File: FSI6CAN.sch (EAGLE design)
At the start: 39 parts, among them IC2 TCAN332DR, IC3 ATMEGA328P, IC4 MCP2515

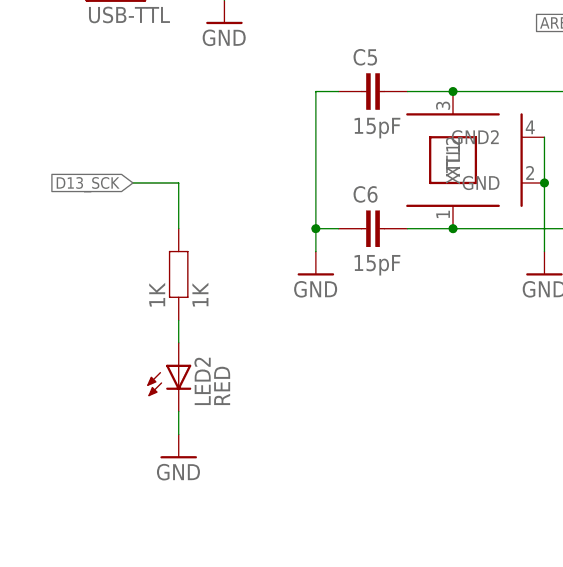
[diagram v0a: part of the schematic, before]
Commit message: Fixed value of R10
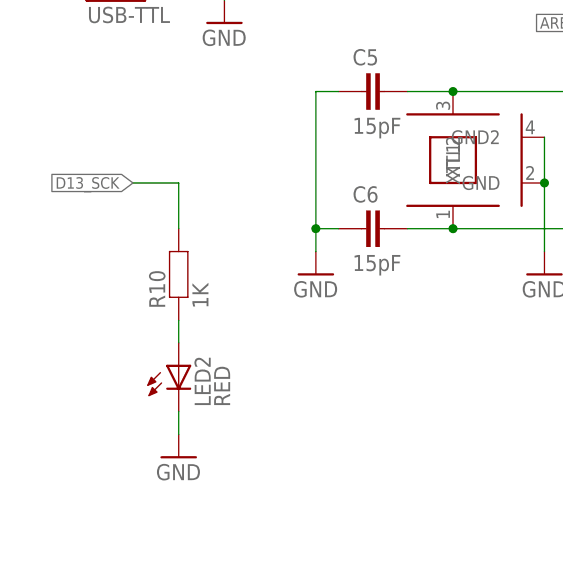
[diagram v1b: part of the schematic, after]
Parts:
- renumbered 1K to R10
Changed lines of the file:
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@@
 <?xml version="1.0" encoding="utf-8"?>
 <!DOCTYPE eagle SYSTEM "eagle.dtd">
-<eagle version="9.5.0">
+<eagle version="9.5.2">
 <drawing>
 <settings>
@@
 <part name="LED2" library="SuperHouse-LEDs" library_urn="urn:adsk.eagle:library:11790571" deviceset="LED" device="0603" package3d_urn="urn:adsk.eagle:package:7066240/3" value="RED"/>
 <part name="GND12" library="SuperHouse-SupplySymbols" library_urn="urn:adsk.eagle:library:11790503" deviceset="GND" device=""/>
-<part name="1K" library="SuperHouse-DiscreteSemi" library_urn="urn:adsk.eagle:library:11768461" deviceset="RESISTOR" device="0603" package3d_urn="urn:adsk.eagle:package:11768543/2" value="1K"/>
+<part name="R10" library="SuperHouse-DiscreteSemi" library_urn="urn:adsk.eagle:library:11768461" deviceset="RESISTOR" device="0603" package3d_urn="urn:adsk.eagle:package:11768543/2" value="1K"/>
 <part name="C4" library="SuperHouse-DiscreteSemi" library_urn="urn:adsk.eagle:library:11768461" deviceset="CAP" device="0603" package3d_urn="urn:adsk.eagle:package:7066315/6" value="1uF"/>
 <part name="R6" library="SuperHouse-DiscreteSemi" library_urn="urn:adsk.eagle:library:11768461" deviceset="RESISTOR" device="0603" package3d_urn="urn:adsk.eagle:package:11768543/2" value="120R"/>
@@
 <attribute name="VALUE" x="20.32" y="35.56" size="1.778" layer="96"/>
 </instance>
-<instance part="1K" gate="G$1" x="22.86" y="58.42" smashed="yes" rot="R90">
+<instance part="R10" gate="G$1" x="22.86" y="58.42" smashed="yes" rot="R90">
 <attribute name="NAME" x="21.3614" y="54.61" size="1.778" layer="95" rot="R90"/>
 <attribute name="VALUE" x="26.162" y="54.61" size="1.778" layer="96" rot="R90"/>
@@
 <segment>
 <pinref part="LED2" gate="G$1" pin="A"/>
-<pinref part="1K" gate="G$1" pin="1"/>
+<pinref part="R10" gate="G$1" pin="1"/>
 <wire x1="22.86" y1="53.34" x2="22.86" y2="50.8" width="0.1524" layer="91"/>
 </segment>
@@
 </segment>
 <segment>
-<pinref part="1K" gate="G$1" pin="2"/>
+<pinref part="R10" gate="G$1" pin="2"/>
 <wire x1="22.86" y1="63.5" x2="22.86" y2="68.58" width="0.1524" layer="91"/>
 <wire x1="22.86" y1="68.58" x2="17.78" y2="68.58" width="0.1524" layer="91"/>
